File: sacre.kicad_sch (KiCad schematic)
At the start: 46 parts, among them J1 Touch, J2 Screen, M1 Vibration_Motor, Q1 CJ2312, Q2 S8050, Q3 CJ3415, Q4 SI1308EDL, U1 LIS3DH, U2 ESP32-PICO-D4, Y1 RV-8803-C7-TA-QC

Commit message: Guarda el estado actual del diseño KiCad
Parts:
- added H1, H2, H3, H4: MountingHole, MountingHole:MountingHole_2.7mm_M2.5, symbol Mechanical:MountingHole
- J1: footprint Connector_FFC-FPC:Hirose_FH12-6S-0.5SH_1x06-1MP_P0.50mm_Horizontal -> EasyEDA:FPC-SMD_P0.50-6P_QCHF-SM-H2.0
- J2: footprint Connector_FFC:524352471TR250 -> EasyEDA:FPC-SMD_P0.50-24P_QCHF-SM-H2.0
- L1: footprint LQH44PN100MP0L:LQH44PN100MP0L -> Inductor_SMD:L_Vishay_IFSC-1515AH_4x4x1.8mm
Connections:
- net +3V3: now also J1.5 (Pin_5); no longer J1.2 (Pin_2)
- net GND: now also J1.6 (Pin_6); no longer J1.1 (Pin_1)
- net INT_TOUCH: now also J1.3 (Pin_3); no longer J1.4 (Pin_4)
- net SCL: now also J1.2 (Pin_2); no longer J1.5 (Pin_5)
- net SDA: now also J1.1 (Pin_1); no longer J1.6 (Pin_6)
- net at JP1.1 (A), R11.2: now also J1.4 (Pin_4); no longer J1.3 (Pin_3)
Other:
- note added: "GDEY042T81-T02"
- note added: "REVISION NOTES: - Touch FPC: SDA and SCL are swapped. Correct TOUCH_SDA/TOUCH_SCL routing in next revision. - Touch FPC: improve mechanical clearance and flex cable exit/orientation. - Vibration motor Q2: selected S8050 SOT-23 pinout does not match PCB pad mapping. Fix Q2 symbol/footprint or select a pin-compatible driver transistor. - Pullup en int touch - Más condensadorees cerca del mcu"
- note added: "https://ae01.alicdn.com/kf/S5c3e0b255ffe41919954e65f1d952eb1L.jpg"
- note added: "https://buy-lcd.com/products/gdey042t81-t02"

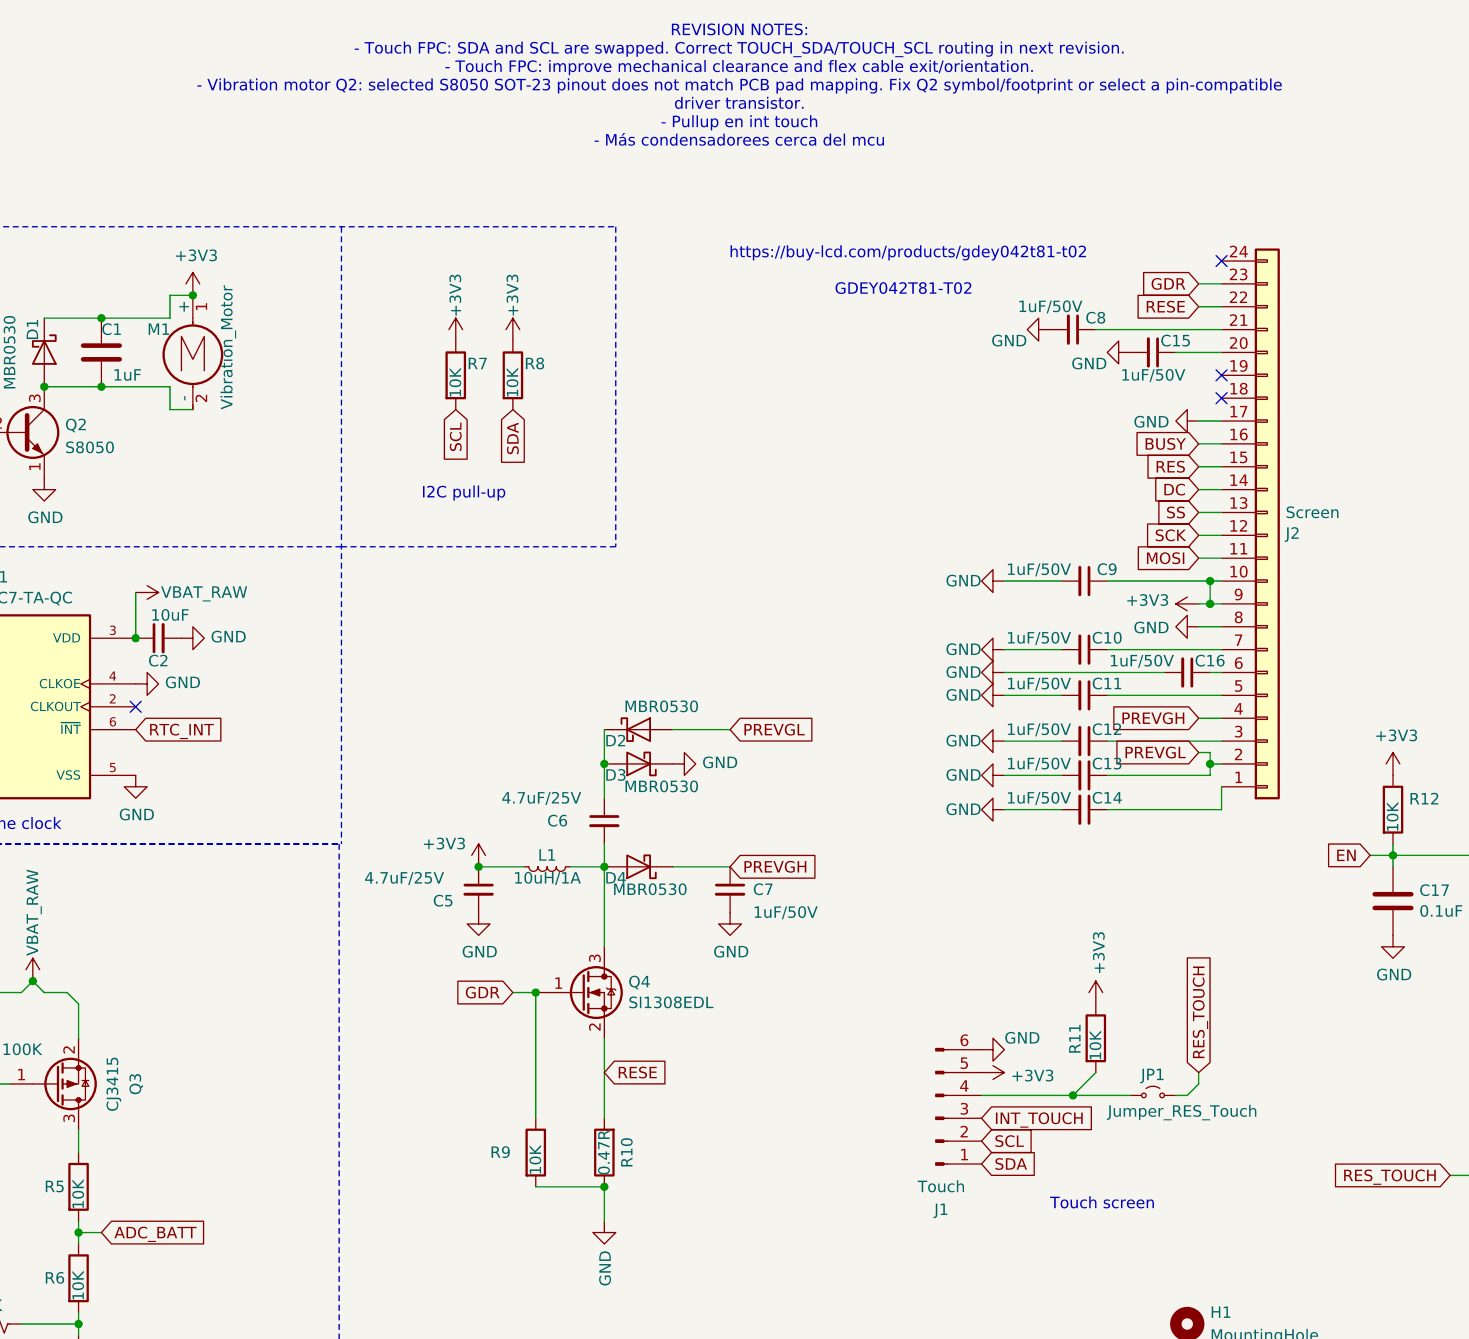
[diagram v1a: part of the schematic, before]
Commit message: Corrige SDA y SCL del conector táctil
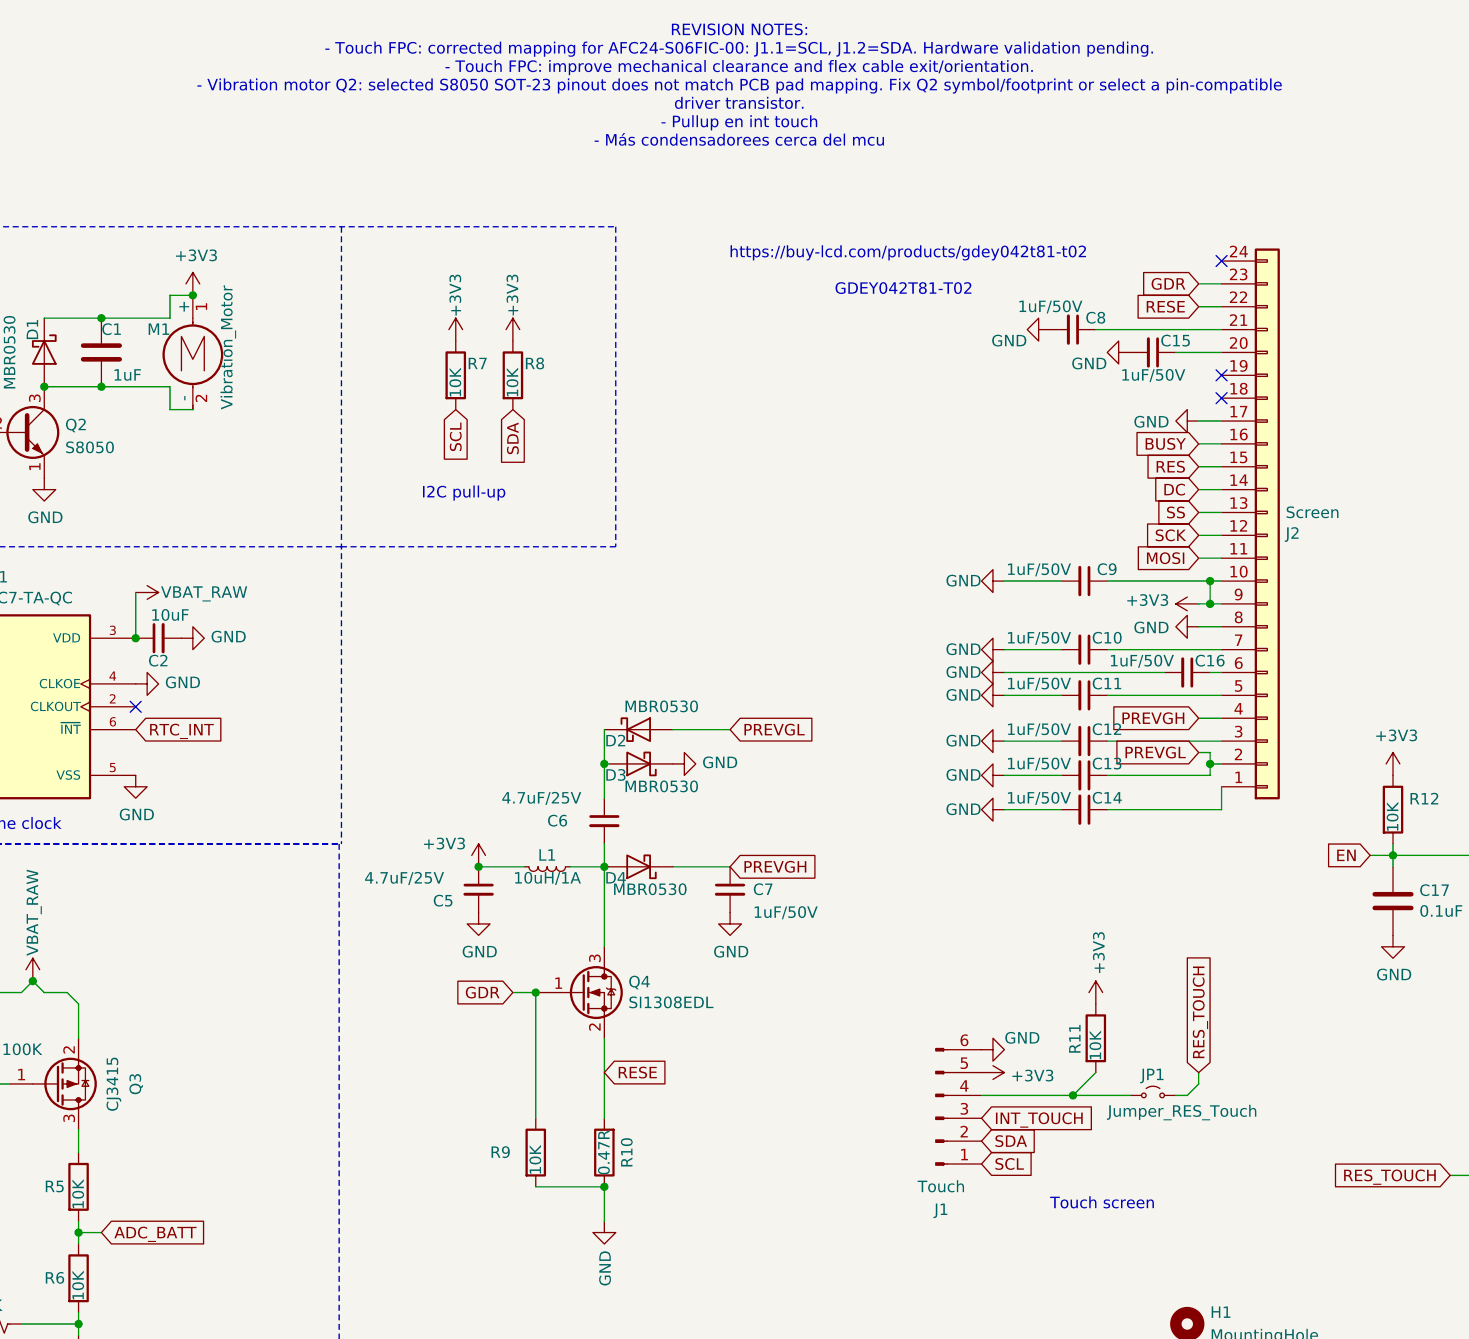
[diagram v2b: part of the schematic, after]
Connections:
- net SCL: now also J1.1 (Pin_1); no longer J1.2 (Pin_2)
- net SDA: now also J1.2 (Pin_2); no longer J1.1 (Pin_1)
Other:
- note added: "REVISION NOTES: - Touch FPC: corrected mapping for AFC24-S06FIC-00: J1.1=SCL, J1.2=SDA. Hardware validation pending. - Touch FPC: improve mechanical clearance and flex cable exit/orientation. - Vibration motor Q2: selected S8050 SOT-23 pinout does not match PCB pad mapping. Fix Q2 symbol/footprint or select a pin-compatible driver transistor. - Pullup en int touch - Más condensadorees cerca del m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"
- note removed: "REVISION NOTES: - Touch FPC: SDA and SCL are swapped. Correct TOUCH_SDA/TOUCH_SCL routing in next revision. - Touch FPC: improve mechanical clearance and flex cable exit/orientation. - Vibration motor Q2: selected S8050 SOT-23 pinout does not match PCB pad mapping. Fix Q2 symbol/footprint or select a pin-compatible driver transistor. - Pullup en int touch - Más condensadorees cerca del mcu"

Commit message: Consolida correcciones eléctricas y documentación
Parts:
- removed C16, C8: 1uF/50V, Capacitor_SMD:C_0603_1608Metric, symbol SmartFeedback-rescue:C_Small-Device
- added C25, C26: 10uF, Capacitor_SMD:C_0603_1608Metric, symbol SmartFeedback-rescue:C_Small-Device
- added C27: 0.1uF, Capacitor_SMD:C_0603_1608Metric, symbol SmartFeedback-rescue:C_Small-Device
- added C30: 100nF, Capacitor_SMD:C_0603_1608Metric, symbol SmartFeedback-rescue:C_Small-Device
- added D8, D9: MBR0530, Diode_SMD:D_SOD-123, symbol SmartFeedback-rescue:MBR0530-Diode
- added R21, R25: 100K, Resistor_SMD:R_0603_1608Metric, symbol SmartFeedback-rescue:R-Device
- added R22: 10K, Resistor_SMD:R_0603_1608Metric, symbol SmartFeedback-rescue:R-Device
- AE1: LCSC Part # (none) -> C5943777
- C1: value 1uF -> 0.1uF; LCSC Part # (none) -> C14663
- C10, C11, C12, C13, C14, C15, C7, C9: LCSC Part # (none) -> C15849
- C17: value 0.1uF -> 1uF; LCSC Part # (none) -> C15849
- C2: value 10uF -> 0.1uF; LCSC Part # (none) -> C14663
- C3: LCSC Part # (none) -> C14663
- C4: LCSC Part # (none) -> C19702
- C5, C6: LCSC Part # (none) -> C69335
- D1: LCSC Part # (none) -> C77336
- D2, D3, D4: LCSC Part # (none) -> C236079
- J1: LCSC Part # (none) -> C262287
- J2: LCSC Part # (none) -> C262683
- L1: value 10uH/1A -> 47uH; footprint Inductor_SMD:L_Vishay_IFSC-1515AH_4x4x1.8mm -> Inductor_SMD:L_Changjiang_FNR4020S; LCSC Part # (none) -> C843300; MPN (none) -> FHD4020S-470MT; Manufacturer (none) -> cjiang; Murata LQH44PN100MP0L -> (none); Sunltech Tech SLF0403-100MTT -> (none)
- Q1: LCSC Part # (none) -> C23521
- Q2: symbol Transistor_BJT:S8050 -> Transistor_BJT:SS8050; LCSC Part # (none) -> C20069125
- Q3: LCSC Part # (none) -> C2910186
- Q4: LCSC Part # (none) -> C7603347
- R1, R12, R5, R6: LCSC Part # (none) -> C25804
- R10: value 0.47R -> 2.2R; LCSC Part # (none) -> C22939
- R11: value 10K -> 1k; LCSC Part # (none) -> C21190
- R2: LCSC Part # (none) -> C21190
- R3, R4: LCSC Part # (none) -> C25803
- R7, R8: value 10K -> 5.1k; LCSC Part # (none) -> C23186
- R9: value 10K -> 1M0; LCSC Part # (none) -> C22935
- TP1: renamed from JP1; value Jumper_RES_Touch -> RTC_EVI; footprint Jumper:SolderJumper-2_P1.3mm_Open_TrianglePad1.0x1.5mm -> TestPoint:TestPoint_Pad_D1.0mm; symbol Jumper:Jumper_2_Small_Open -> Connector:TestPoint; now left out of the parts list
- U1: LCSC Part # (none) -> C15134
- U2: LCSC Part # (none) -> C193707
- Y1: LCSC Part # (none) -> C2846926
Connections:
- net +3V3: now also C26.1, C27.1, D8.1 (K), R22.1; no longer C1.1, D1.1 (K), M1.1 (+), R11.1
- net ACC_INT2: now also U2.10 (IO34); no longer U2.18 (IO12)
- net GND: now also Q2.2 (E), C25.2, C26.2, C27.2, C30.2, R25.2; no longer Q2.1 (E)
- net RTC_EVI: now also TP1.1, R21.2; no longer U2.21 (IO15)
- net RTC_INT: now also R22.2
- net VBAT_RAW: now also R21.1
- net RES_TOUCH_CTRL: now reaches U2.24 (IO4)
- net RES_TOUCH_CTRL: now also R11.2
- net at U2.26 (VDD_SDIO): now also C30.1
- net at R2.1: now also Q2.1 (B), R25.1; no longer Q2.2 (B)
- net GPO: no longer names the net of U2.12 (IO32)
- net RES_TOUCH: no longer names the net of U2.25 (IO16)
- net RES_TOUCH: no longer TP1.2 (B)
- new net: C25.1, D8.2 (A), J1.4 (Pin_4), R11.1
- new net VMOTOR: C1.1, D1.1 (K), D9.1 (K), M1.1 (+)
- new net VSYS: D9.2 (A)
- no-connect marks 21 -> 24
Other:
- note added: "ACELERÓMETRO LIS3DH"
- note added: "BOOSTER SSD1683: L1=47 µH y R10=2.2 Ω según GDEY042T81-T02. No restaurar los valores de la versión antigua de pantalla."
- note added: "BUS I²C: R7/R8=5.1 kΩ. Usar 100 kHz hasta validar 400 kHz con la PCB y el flex conectados."
- note added: "COLOCAR JUNTO A U1.14"
- note added: "DESACOPLO ESP32-PICO-D4: C27 (100 nF) junto a los pines 1/3/4 de U2; C26 (10 µF) junto a C27. Mantener cortas la alimentación y su retorno GND."
- note added: "GPIO13: LOW=OFF; HIGH=ON; PWM opcional. D9 reduce VMOTOR con batería a 4,2 V."
- note added: "MEDIDA DE BATERÍA: GPIO26 HIGH habilita el divisor; leer ADC_BATT y volver a LOW. Apagar antes de brownout repetido; fijar el umbral por medida."
- note added: "MOTOR CANDIDATO: 3 V; 70 mA nominales; 90 mA de arranque. https://es.aliexpress.com/item/1005007550657082.html"
- note added: "PANEL GDEY042T81-T02: https://buy-lcd.com/products/gdey042t81-t02"
- note added: "RESET TÁCTIL (GPIO4): Forzar LOW en open-drain durante >=60 ms y después liberar. No conducir HIGH; esperar >=300 ms antes de usar I²C."
- note added: "RF: CONEXIÓN DIRECTA DE 50 Ω, DECISIÓN ACEPTADA. AE1=AN012400C00; pista corta, uniforme, sin vías y con retorno continuo. Sin red π: no se montan valores de adaptación sin medida RF. Una revisión futura puede añadirla y ajustarla con VNA."
- note added: "RTC: Y1 permanece alimentado desde VBAT_RAW con el equipo apagado. INT es open-drain y necesita R22. EVI es una entrada opcional: R21 la mantiene HIGH; TP1 permite usarla en el futuro."
- note removed: "(Close to pin 14 U1)"
- note removed: "Accelerometer"
- note removed: "Battery level measurement"
- note removed: "I2C pull-up"
- note removed: "REVISION NOTES: - Touch FPC: corrected mapping for AFC24-S06FIC-00: J1.1=SCL, J1.2=SDA. Hardware validation pending. - Touch FPC: improve mechanical clearance and flex cable exit/orientation. - Vibration motor Q2: selected S8050 SOT-23 pinout does not match PCB pad mapping. Fix Q2 symbol/footprint or select a pin-compatible driver transistor. - Pullup en int touch - Más condensadorees cerca del m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"
- note removed: "Real time clock"
- note removed: "https://ae01.alicdn.com/kf/S5c3e0b255ffe41919954e65f1d952eb1L.jpg"
- note removed: "https://buy-lcd.com/products/gdey042t81-t02"
- moved on the sheet: R11, R2

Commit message: Aclara notas del esquema y valida salida de 3V3
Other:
- note added: "BOOSTER DEL PANEL: Este bloque sigue la aplicación específica GDEY042T81-T02, no la genérica del SSD1683. R9 es el pull-down de GDR; C8 y C16 se omiten porque sus pines son NC/prueba."
- note added: "C3/C4: desacoplo local de VDD/VDD_IO. Colocar junto a U1.1/U1.14."
- note added: "CONECTOR TÁCTIL FT6336U"
- note added: "DESACOPLO ESP32-PICO-D4: C27 absorbe ruido de alta frecuencia y debe quedar pegado a U2.1/3/4. C26 aporta reserva local; mantener cortos alimentación y retorno GND."
- note added: "MOTOR CANDIDATO: 3 V y 70 mA nominales. Verificar la corriente de arranque del lote antes de fabricar. https://es.aliexpress.com/item/1005007550657082.html"
- note added: "MOTOR DE 3 V: D9 reduce VSYS para no aplicarle hasta 4,2 V. GPIO13: LOW=OFF, HIGH=ON; PWM sólo para regular intensidad."
- note added: "RESET FT6336U: C25 retrasa unos 30 ms; D8 descarga el nodo al apagar. GPIO4: open-drain LOW >=60 ms y después alta impedancia. Esperar >=300 ms antes de usar I²C."
- note added: "RTC: Y1 usa VBAT_RAW para conservar la hora con el latch apagado. R22 lleva INT al dominio +3V3; no sustituirlo por un pull-up a VBAT_RAW. EVI no se usa: R21 la mantiene HIGH y TP1 permite recuperarla en el futuro."
- note added: "VELOCIDAD I²C: usar 100 kHz por defecto. Usar 400 kHz sólo tras validar los flancos con la PCB y el flex conectados."
- note removed: "BOOSTER SSD1683: L1=47 µH y R10=2.2 Ω según GDEY042T81-T02. No restaurar los valores de la versión antigua de pantalla."
- note removed: "BUS I²C: R7/R8=5.1 kΩ. Usar 100 kHz hasta validar 400 kHz con la PCB y el flex conectados."
- note removed: "COLOCAR JUNTO A U1.14"
- note removed: "DESACOPLO ESP32-PICO-D4: C27 (100 nF) junto a los pines 1/3/4 de U2; C26 (10 µF) junto a C27. Mantener cortas la alimentación y su retorno GND."
- note removed: "GDEY042T81-T02"
- note removed: "GPIO13: LOW=OFF; HIGH=ON; PWM opcional. D9 reduce VMOTOR con batería a 4,2 V."
- note removed: "MOTOR CANDIDATO: 3 V; 70 mA nominales; 90 mA de arranque. https://es.aliexpress.com/item/1005007550657082.html"
- note removed: "RESET TÁCTIL (GPIO4): Forzar LOW en open-drain durante >=60 ms y después liberar. No conducir HIGH; esperar >=300 ms antes de usar I²C."
- note removed: "RTC: Y1 permanece alimentado desde VBAT_RAW con el equipo apagado. INT es open-drain y necesita R22. EVI es una entrada opcional: R21 la mantiene HIGH; TP1 permite usarla en el futuro."
- note removed: "Touch screen"
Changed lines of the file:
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@@
 		)
 	)
-	(text "COLOCAR JUNTO A U1.14"
+	(text "C3/C4: desacoplo local de VDD/VDD_IO.\nColocar junto a U1.1/U1.14."
 		(exclude_from_sim no)
-		(at 82.55 172.72 0)
+		(at 60.96 157.48 0)
 		(effects
 			(font
-				(size 0.9906 0.9906)
+				(size 0.7 0.7)
 			)
 			(justify left bottom)
@@
 		)
 	)
-	(text "Touch screen"
+	(text "CONECTOR TÁCTIL FT6336U"
 		(exclude_from_sim no)
 		(at 170.18 125.73 0)
@@
 		)
 	)
-	(text "MOTOR CANDIDATO: 3 V; 70 mA nominales; 90 mA de arranque.\nhttps://es.aliexpress.com/item/1005007550657082.html"
+	(text "MOTOR CANDIDATO: 3 V y 70 mA nominales.\nVerificar la corriente de arranque del lote antes de fabricar.\nhttps://es.aliexpress.com/item/1005007550657082.html"
 		(exclude_from_sim no)
 		(at 196.342 164.084 0)
@@
 		)
 	)
-	(text "BUS I²C: R7/R8=5.1 kΩ.\nUsar 100 kHz hasta validar 400 kHz con la PCB y el flex conectados."
+	(text "VELOCIDAD I²C: usar 100 kHz por defecto.\nUsar 400 kHz sólo tras validar los flancos con la PCB y el flex conectados."
 		(exclude_from_sim no)
 		(at 102.87 44.45 0)
@@
 		)
 	)
-	(text "RTC: Y1 permanece alimentado desde VBAT_RAW con el equipo apagado.\nINT es open-drain y necesita R22.\nEVI es una entrada opcional: R21 la mantiene HIGH; TP1 permite usarla en el futuro."
+	(text "RTC: Y1 usa VBAT_RAW para conservar la hora con el latch apagado.\nR22 lleva INT al dominio +3V3; no sustituirlo por un pull-up a VBAT_RAW.\nEVI no se usa: R21 la mantiene HIGH y TP1 permite recuperarla en el futuro."
 		(exclude_from_sim no)
 		(at 21.336 82.042 0)
@@
 		)
 	)
-	(text "DESACOPLO ESP32-PICO-D4:\nC27 (100 nF) junto a los pines 1/3/4 de U2; C26 (10 µF) junto a C27.\nMantener cortas la alimentación y su retorno GND."
+	(text "DESACOPLO ESP32-PICO-D4:\nC27 absorbe ruido de alta frecuencia y debe quedar pegado a U2.1/3/4.\nC26 aporta reserva local; mantener cortos alimentación y retorno GND."
 		(exclude_from_sim no)
 		(at 203.2 52.07 0)
@@
 		)
 	)
-	(text "GPIO13: LOW=OFF; HIGH=ON; PWM opcional.\nD9 reduce VMOTOR con batería a 4,2 V."
+	(text "MOTOR DE 3 V: D9 reduce VSYS para no aplicarle hasta 4,2 V.\nGPIO13: LOW=OFF, HIGH=ON; PWM sólo para regular intensidad."
 		(exclude_from_sim no)
-		(at 20.828 28.956 0)
+		(at 20.32 45.72 0)
 		(effects
 			(font
-				(size 1 1)
+				(size 0.8 0.8)
 			)
 			(justify left bottom)
 		)
 	)
-	(text "BOOSTER SSD1683: L1=47 µH y R10=2.2 Ω según GDEY042T81-T02.\nNo restaurar los valores de la versión antigua de pantalla."
+	(text "BOOSTER DEL PANEL:\nEste bloque sigue la aplicación específica GDEY042T81-T02, no la genérica del SSD1683.\nR9 es el pull-down de GDR; C8 y C16 se omiten porque sus pines son NC/prueba."
 		(exclude_from_sim no)
 		(at 102.362 135.382 0)
@@
 		)
 	)
-	(text "GDEY042T81-T02"
-		(exclude_from_sim no)
-		(at 156.464 21.082 0)
-		(effects
-			(font
-				(size 1.27 1.27)
-			)
-		)
-	)
-	(text "COLOCAR JUNTO A U1.14"
-		(exclude_from_sim no)
-		(at 82.55 182.88 0)
-		(effects
-			(font
-				(size 0.9906 0.9906)
-			)
-			(justify left bottom)
-		)
-	)
-	(text "RESET TÁCTIL (GPIO4):\nForzar LOW en open-drain durante >=60 ms y después liberar.\nNo conducir HIGH; esperar >=300 ms antes de usar I²C."
+	(text "RESET FT6336U:\nC25 retrasa unos 30 ms; D8 descarga el nodo al apagar.\nGPIO4: open-drain LOW >=60 ms y después alta impedancia.\nEsperar >=300 ms antes de usar I²C."
 		(exclude_from_sim no)
 		(at 154.94 129.54 0)
 		(effects
 			(font
-				(size 1.27 1.27)
+				(size 0.8 0.8)
 			)
 			(justify left)
